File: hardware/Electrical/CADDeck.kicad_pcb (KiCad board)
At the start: 2 copper layers, 129 x 82.5 mm, 46 parts, among them J1 Conn_01x05_Socket, J4 Conn_01x04_Socket, J5 Conn_01x10_Socket, Q1 2N2222, SW1 SW_Push, SW10 SW_Push, SW2 SW_Push, SW3 SW_Push, SW4 SW_Push, SW5 SW_Push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

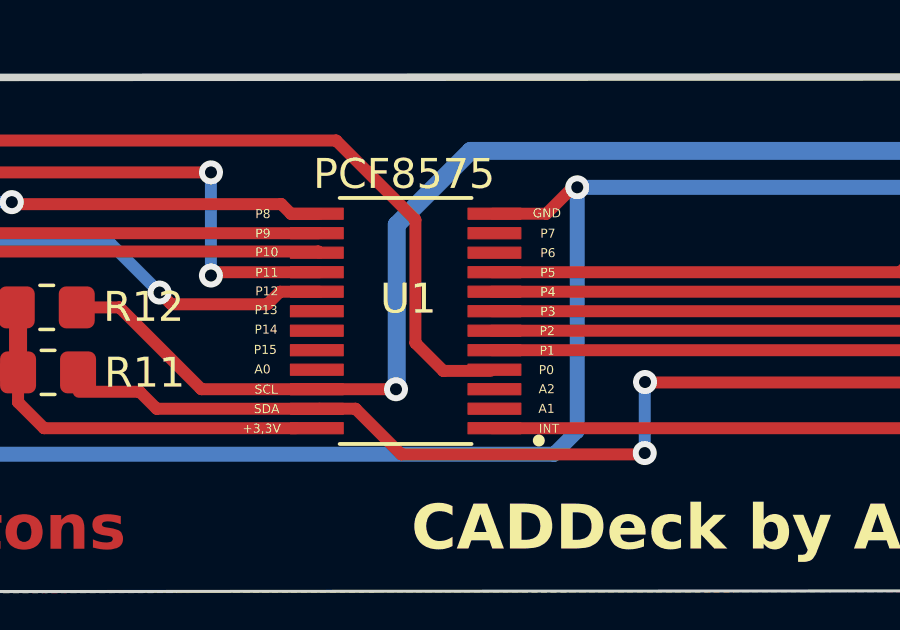
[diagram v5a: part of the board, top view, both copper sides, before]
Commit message: PCG8575 A0-A1 auf GND gelegt
Muss noch getestet werden, da der PCF nicht funktionierte.
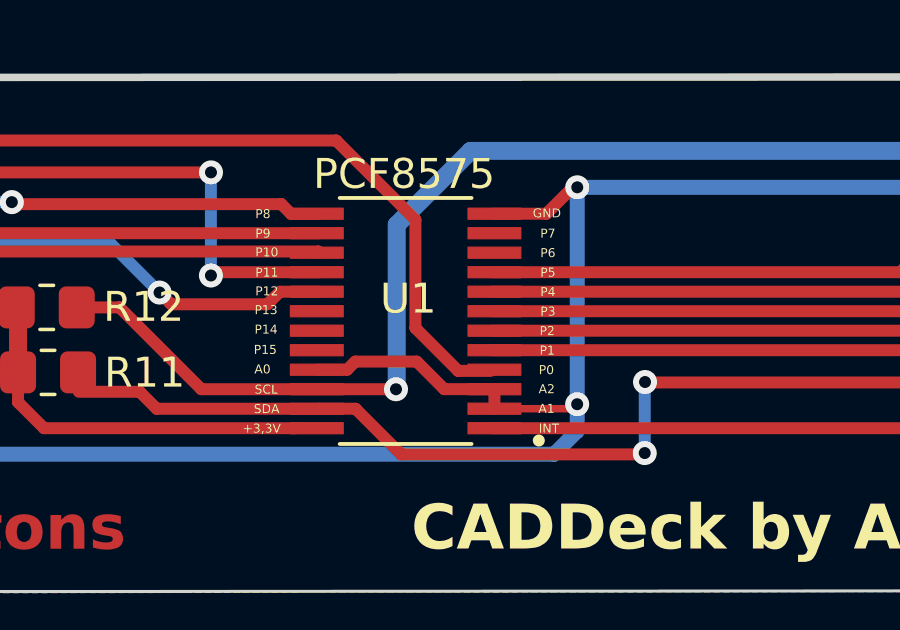
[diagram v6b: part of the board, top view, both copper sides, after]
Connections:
- U1 pad 2: unconnected-(U1-A1-Pad2) -> GND
- U1 pad 21: unconnected-(U1-A0-Pad21) -> GND
- U1 pad 3: unconnected-(U1-A2-Pad3) -> GND
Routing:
- net GND: track 338.4 -> 348.4 mm, vias 1 -> 2

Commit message: Stückliste ergänzt
Und kleine Optimierungen
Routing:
- net Net-(J1-Pin_3): track 120.0 -> 119.2 mm
- net +3.3V: track 348.6 -> 347.8 mm
